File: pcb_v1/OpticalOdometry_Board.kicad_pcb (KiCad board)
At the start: 2 copper layers, 28 x 28 mm, 13 parts

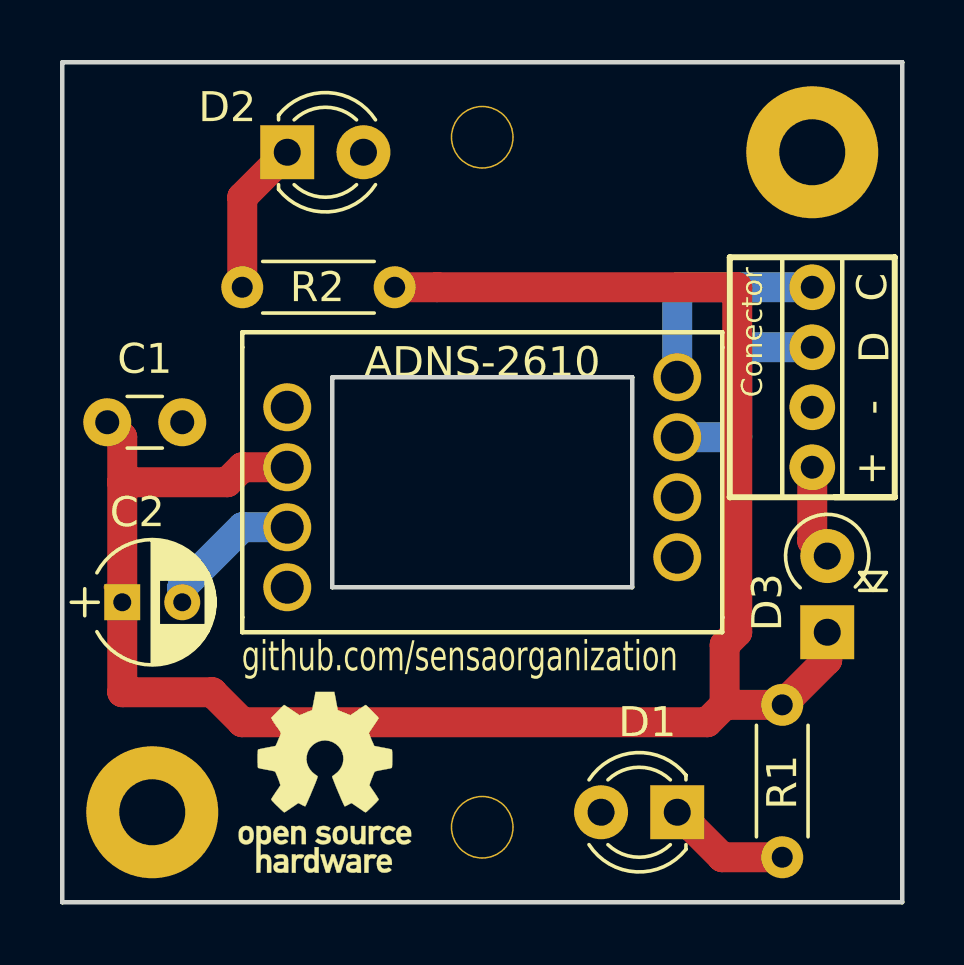
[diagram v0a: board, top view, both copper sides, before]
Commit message: Added logos to the board and the folder
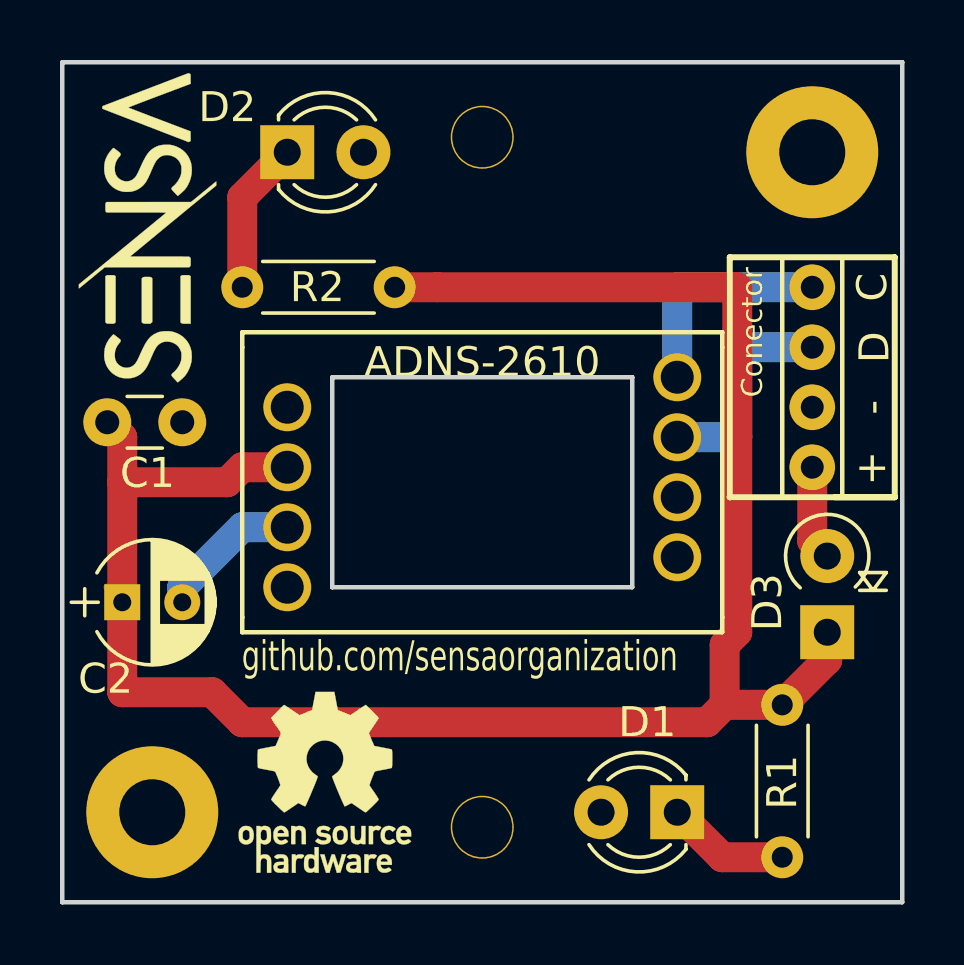
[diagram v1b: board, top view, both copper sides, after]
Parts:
- added G***: LOGO, logo:sensa_logo_10x6, F.Cu at (156.8, 75.9)
